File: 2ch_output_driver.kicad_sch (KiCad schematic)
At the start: 4 parts, among them J12 OUT ${CH_N}, U14 ADuM1201AR

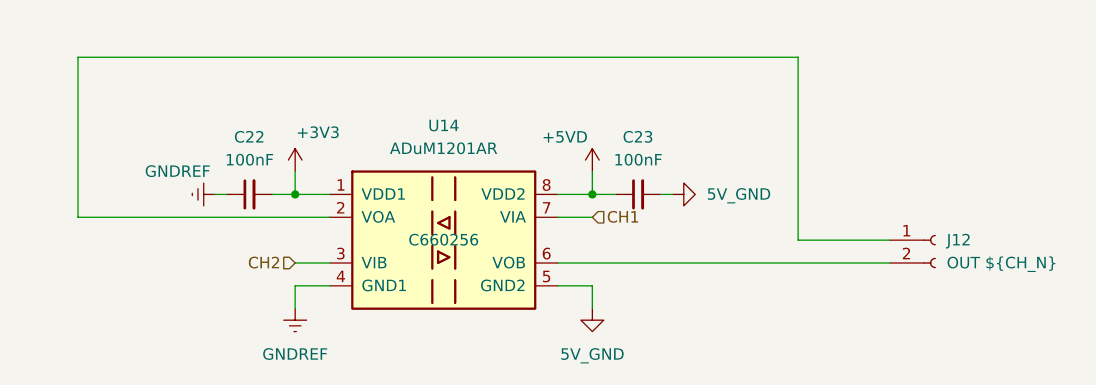
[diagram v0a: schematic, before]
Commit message: Found a bug in the circuit, using the wrong isolated tranceivers, fixed.
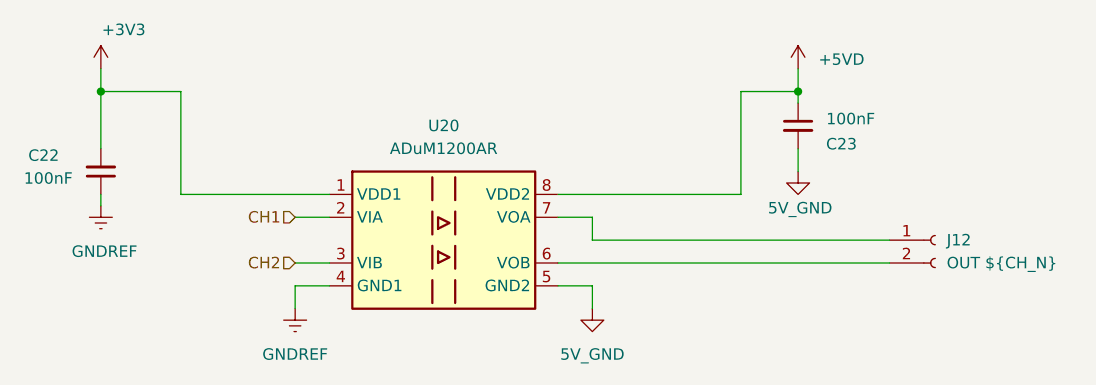
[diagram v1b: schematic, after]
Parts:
- removed U14: ADuM1201AR, Package_SO:SOIC-8_3.9x4.9mm_P1.27mm, symbol Isolator:ADuM1201AR
- added U20: ADuM1200AR, Package_SO:SOIC-8_3.9x4.9mm_P1.27mm, symbol Isolator:ADuM1200AR
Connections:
- net +3V3: now also U20.1 (VDD1)
- net +5VD: now also U20.8 (VDD2)
- net 5V_GND: now also U20.5 (GND2)
- net CH1: now also U20.2 (VIA)
- net CH2: now also U20.3 (VIB)
- net GNDREF: now also U20.4 (GND1)
- net at J12.1 (Pin_1): now also U20.7 (VOA)
- net at J12.2 (Pin_2): now also U20.6 (VOB)
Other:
- moved on the sheet: C22, C23
